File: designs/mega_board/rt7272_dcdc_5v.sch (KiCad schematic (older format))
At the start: 13 parts, among them U3 RT7272

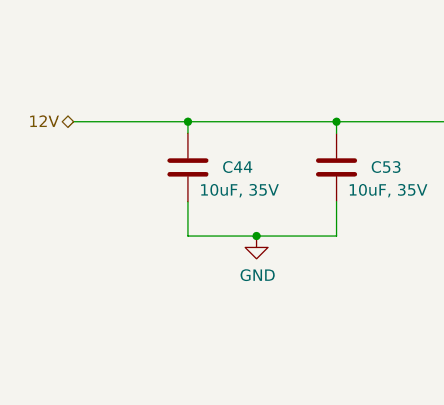
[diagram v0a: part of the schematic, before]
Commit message: renamed net from +12V to VCC
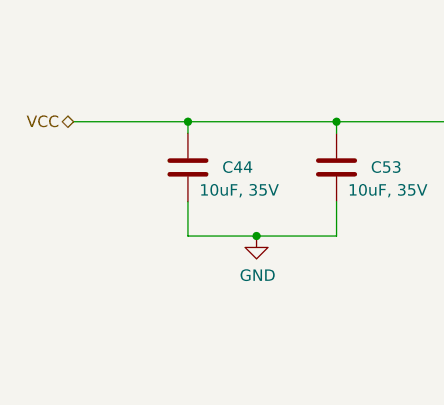
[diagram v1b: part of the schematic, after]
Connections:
- net 12V renamed VCC
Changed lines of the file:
@@
 $Descr A4 11693 8268
 encoding utf-8
-Sheet 8 14
+Sheet 7 14
 Title ""
 Date ""
@@
 ENABLE
 Text HLabel 1650 3350 0    50   BiDi ~ 0
-12V
+VCC
 Text HLabel 10100 3450 2    50   BiDi ~ 0
 5V
